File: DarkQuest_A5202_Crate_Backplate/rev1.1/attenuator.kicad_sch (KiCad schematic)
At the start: 3 parts

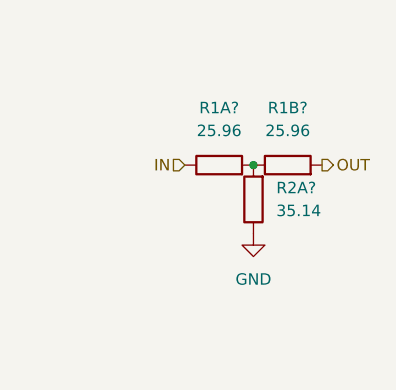
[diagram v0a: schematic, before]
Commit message: Update attenuator.kicad_sch
Replace outdated attenuator schematic with schematic containing rotary switch
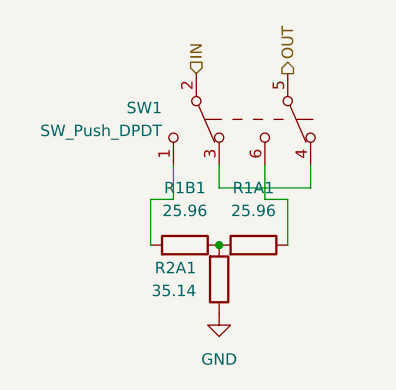
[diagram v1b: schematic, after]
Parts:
- added SW1: SW_Push_DPDT, Relay_SMD:Nidec_DPDT_CS422YTA, symbol Switch:Nidec_DPDT
- gave numbers to parts that had none: 3
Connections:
- net IN: now also SW1.2; no longer R1A1.1
- net OUT: now also SW1.5 (B); no longer R1B1.2
- new net: R1B1.2, SW1.1 (C)
- new net: SW1.3 (A), SW1.4 (A)
- new net: R1A1.1, SW1.6 (0)
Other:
- moved on the sheet: R1A1, R1B1, R2A1

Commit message: Add cmos switches with squashed commits
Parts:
- removed SW1: SW_Push_DPDT, Relay_SMD:Nidec_DPDT_CS422YTA, symbol Switch:Nidec_DPDT
- added C1A1: 0.1u, Capacitor_SMD:C_0402_1005Metric, symbol Device:C
- added SW1: SW_DPDT_x2, A5202_Backplate:Nidec_DPDT_CS422YTA, symbol Switch:SW_DPDT_x2
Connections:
- net GND: now also C1A1.2; no longer R2A1.1
- net IN: now also SW1.2 (B)
- net OUT: now also SW1.5 (B)
- net T_JUNC: now reaches R1A1.2, R1B1.1, R2A1.2
- net R_OUT: now reaches R1B1.2
- net R_OUT: now also SW1.6 (C)
- net R_IN: now reaches R1A1.1
- net R_IN: now also SW1.3 (C)
- new net BYPASSED: SW1.1 (A), SW1.4 (A)
- new net CAP: C1A1.1, R2A1.1
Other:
- note added: "!"
- note added: "DPDT switch symbol has been broken up into 2 units to allow for communication of effective switch locations. It is still 1 footprint and linked as such."
- note added: "△"
- moved on the sheet: R1A1, R1B1, R2A1
